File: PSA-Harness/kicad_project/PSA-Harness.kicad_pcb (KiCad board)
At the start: 4 copper layers, 58.3 x 54 mm, 20 parts, among them J1 to_EPS_1, J10 B2B_1, J11 B2B_2, J2 to_EPS_2, J3 to_ESP_3, J4 to_car_1, J5 to_car_2, J6 to_car_3, J7 USB_C_Receptacle, J8 B2B_1, J9 B2B_2, U1 DG419LEUA, U2 DG419LEUA

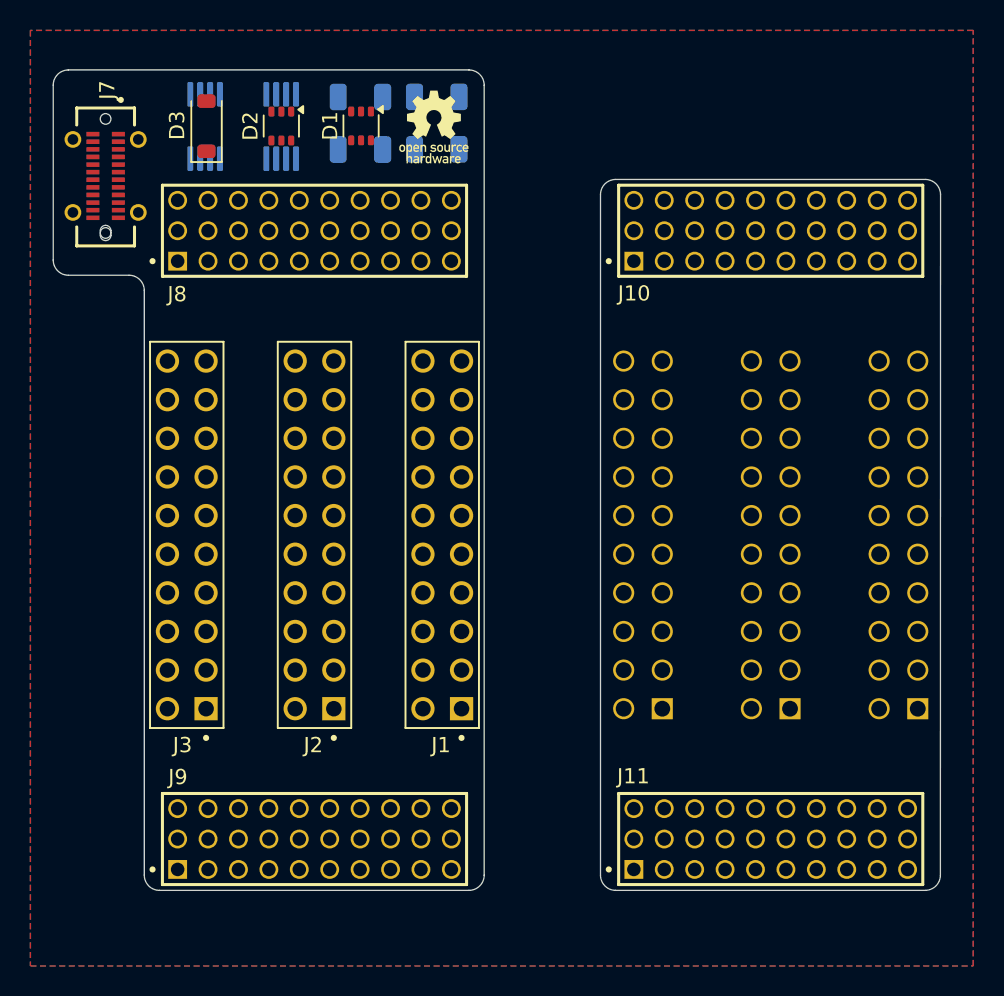
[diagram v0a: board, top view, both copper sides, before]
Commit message: chg: fix component names
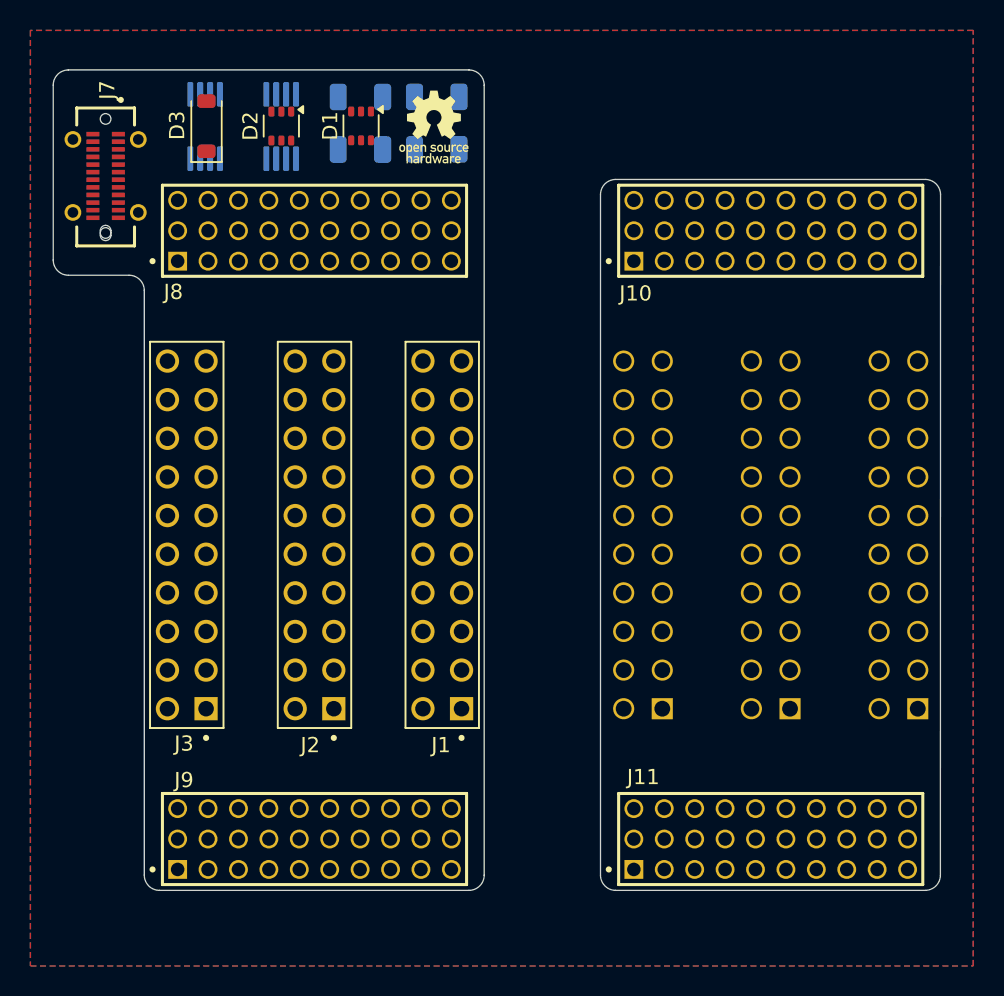
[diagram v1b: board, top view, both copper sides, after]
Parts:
- D1, D2: value BAS40TW-AU -> BAS40SDW
- J1, J2, J3: footprint PSA:10129381-920003BLF -> PSA:Amphenol_10129381-920003BLF
- J10, J11, J8, J9: footprint PSA:SAMTEC_TW-10-X-X-T-X-X -> PSA:SAMTEC_TW-10-03-T-T-320-100
- J4, J5, J6: footprint PSA:ESW-110-44-F-D -> PSA:SAMTEC_ESW-110-44-F-D
- U1, U2: value DG419LEUA -> DG419LEDY-T1-GE4

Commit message: cleanup doc files
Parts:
- U1, U2: value DG419LEDY-T1-GE4 -> DG419LEDQ-T1-GE3
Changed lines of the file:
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@@
 			)
 		)
-		(property "Value" "DG419LEDY-T1-GE4"
+		(property "Value" "DG419LEDQ-T1-GE3"
 			(at 0 -2.45 90)
 			(layer "B.Fab")
@@
 			)
 		)
-		(property "Value" "DG419LEDY-T1-GE4"
+		(property "Value" "DG419LEDQ-T1-GE3"
 			(at 0 -2.45 90)
 			(layer "B.Fab")

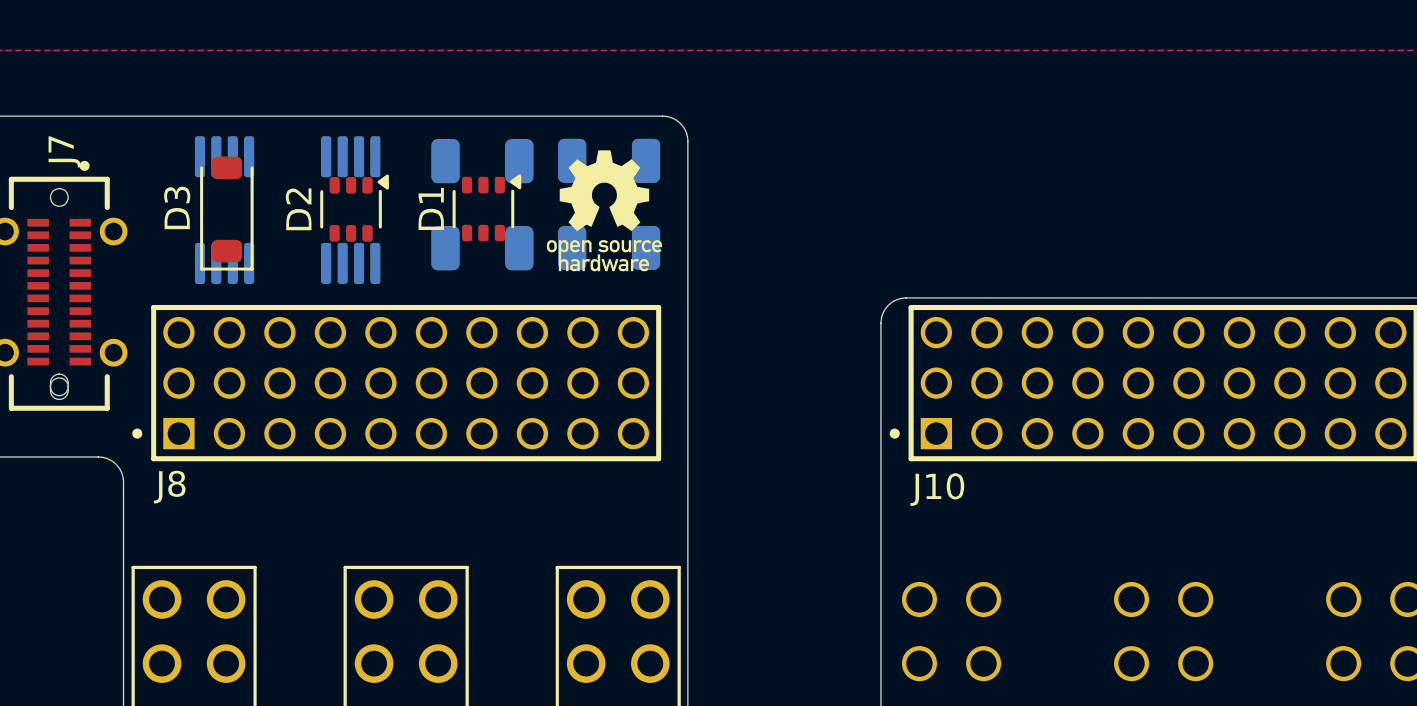
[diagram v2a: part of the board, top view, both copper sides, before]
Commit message: add BOM
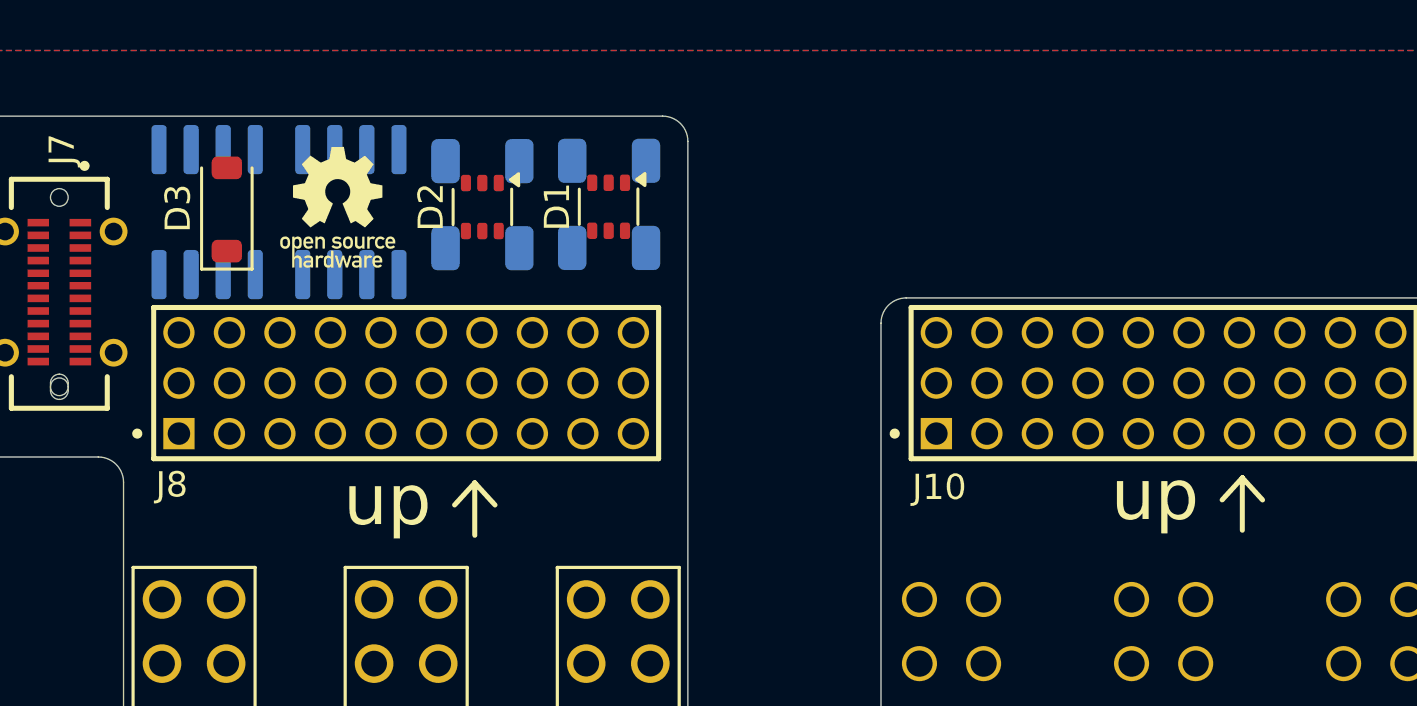
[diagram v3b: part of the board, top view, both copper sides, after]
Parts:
- U1, U2: value DG419LEDQ-T1-GE3 -> DG419LEDQ-T1-GE4; footprint Package_SO:MSOP-8_3x3mm_P0.65mm -> Package_SO:SOIC-8_3.9x4.9mm_P1.27mm
- moved D2 5.20 mm to (108.7, 95.2)
- moved D1 4.96 mm to (113.7, 95.2)
- moved U1 0.69 mm to (97.8, 95.4)
- moved U2 0.08 mm to (103.5, 95.4)
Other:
- board text added: "up"
